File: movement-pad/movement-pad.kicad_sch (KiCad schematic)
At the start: 33 parts, among them U1 74LS147, U2 74LS42

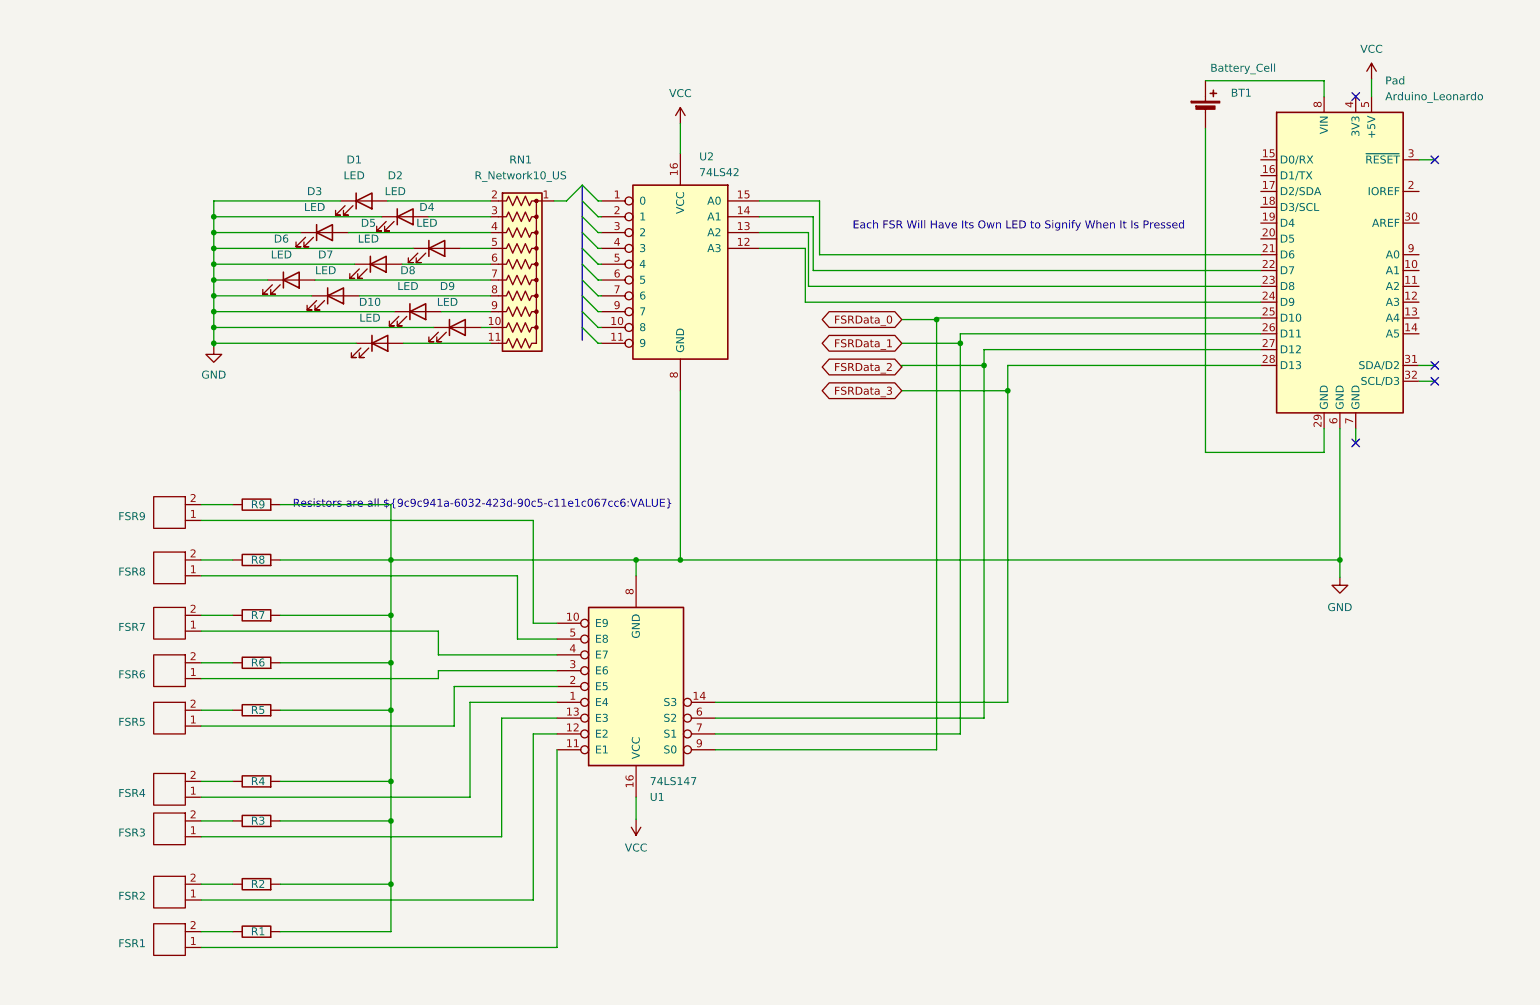
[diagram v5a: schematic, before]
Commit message: realized i screwed up with movement pad, redid it
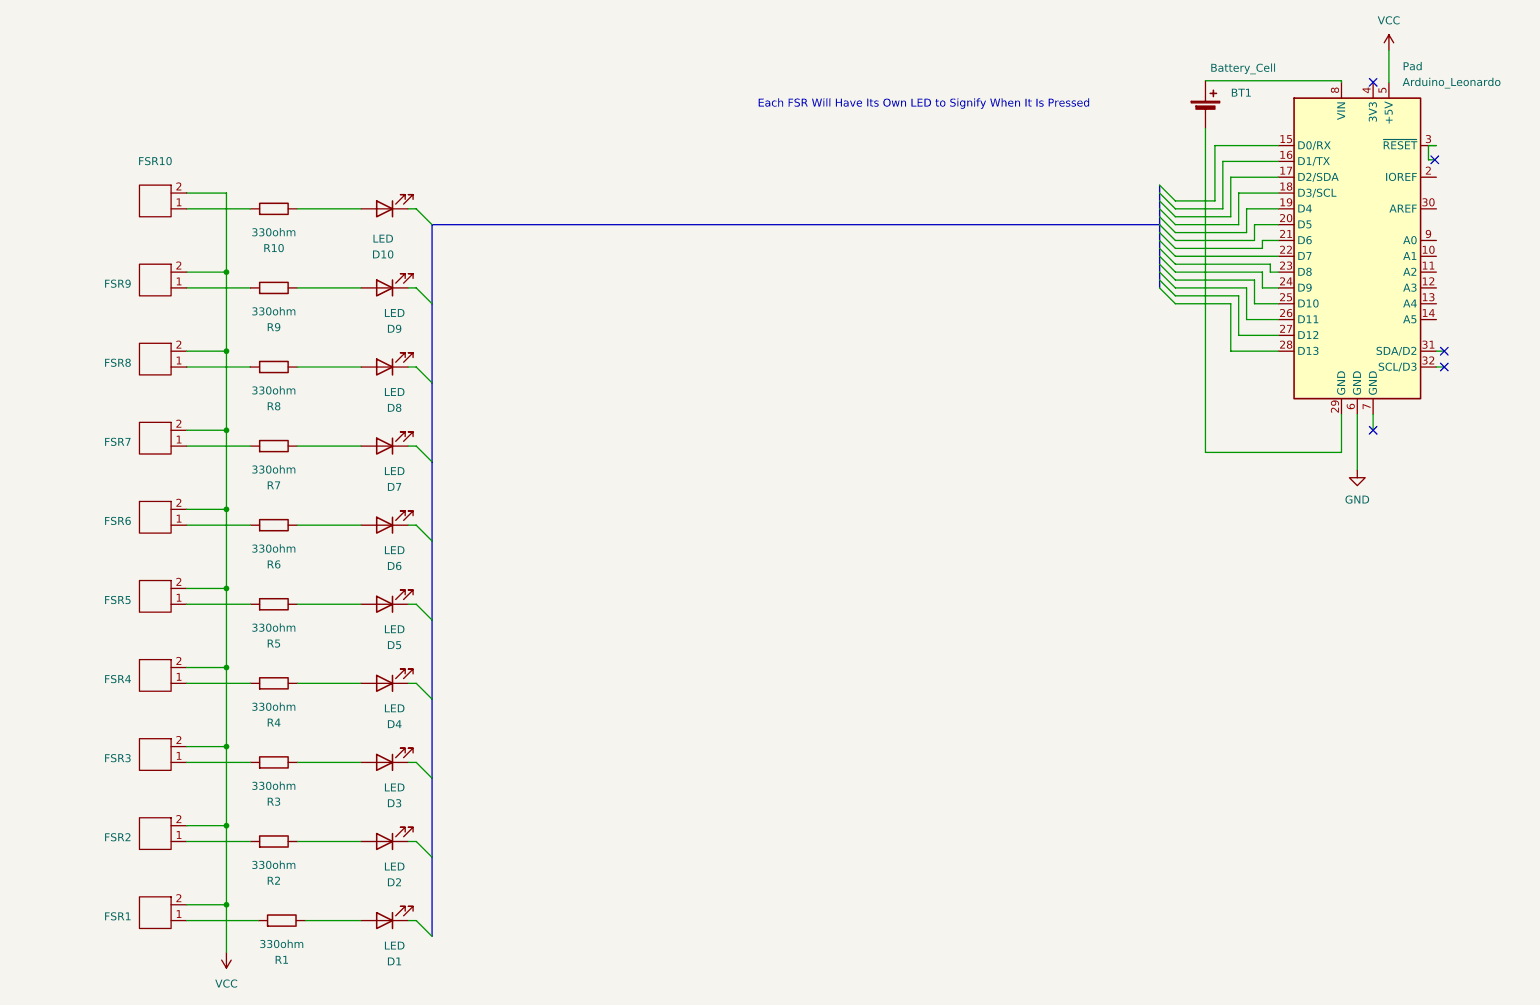
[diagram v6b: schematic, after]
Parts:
- removed R1, R2, R3, R4, R5, R6, R7, R8, R9: 390ohm, Resistor_THT:R_Axial_DIN0207_L6.3mm_D2.5mm_P10.16mm_Horizontal, symbol PCM_SL_Resistors:390ohm
- removed RN1: R_Network10_US, Resistor_THT:R_Array_SIP11, symbol Device:R_Network10_US
- removed U1: 74LS147, symbol 74xx:74LS147
- removed U2: 74LS42, symbol 74xx:74LS42
- added FSR10: ~, symbol GunProject_lib:FSR
- added R1, R10, R2, R3, R4, R5, R6, R7, R8, R9: 330ohm, Resistor_THT:R_Axial_DIN0207_L6.3mm_D2.5mm_P10.16mm_Horizontal, symbol PCM_SL_Resistors:330ohm
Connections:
- net GND: no longer D1.1 (K), D10.1 (K), D2.1 (K), D3.1 (K), D4.1 (K), D5.1 (K), D6.1 (K), D7.1 (K), D8.1 (K), D9.1 (K)
- net VCC: now also FSR1.2, FSR2.2, FSR3.2, FSR4.2, FSR5.2, FSR6.2, FSR7.2, FSR8.2, FSR9.2, FSR10.2
- net at D9.2 (A): now also R9.2
- net at D5.2 (A): now also R5.2
- net at D7.2 (A): now also R7.2
- net at D2.2 (A): now also R2.2
- net at FSR3.1: now also R3.1
- net at FSR4.1: now also R4.1
- net at FSR9.1: now also R9.1
- net at FSR1.1: now also R1.1
- net at FSR2.1: now also R2.1
- net at FSR5.1: now also R5.1
- net at FSR6.1: now also R6.1
- net at FSR7.1: now also R7.1
- net at FSR8.1: now also R8.1
- net at D4.2 (A): now also R4.2
- net at D10.2 (A): now also R10.2
- net at D3.2 (A): now also R3.2
- net at D1.2 (A): now also R1.2
- net at D6.2 (A): now also R6.2
- net at D8.2 (A): now also R8.2
- net FSRData_0: no longer names the net of Pad.25 (D10)
- net FSRData_1: no longer names the net of Pad.26 (D11)
- net FSRData_2: no longer names the net of Pad.27 (D12)
- net FSRData_3: no longer names the net of Pad.28 (D13)
- new net: FSR10.1, R10.1
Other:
- note removed: "Resistors are all ${9c9c941a-6032-423d-90c5-c11e1c067cc6:VALUE}"
- moved on the sheet: D1, D10, D2, D3, D4, D5, D6, D7, D8, D9, FSR1, FSR2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

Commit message: Reworked pad schematic again because the hookup guides are annoying
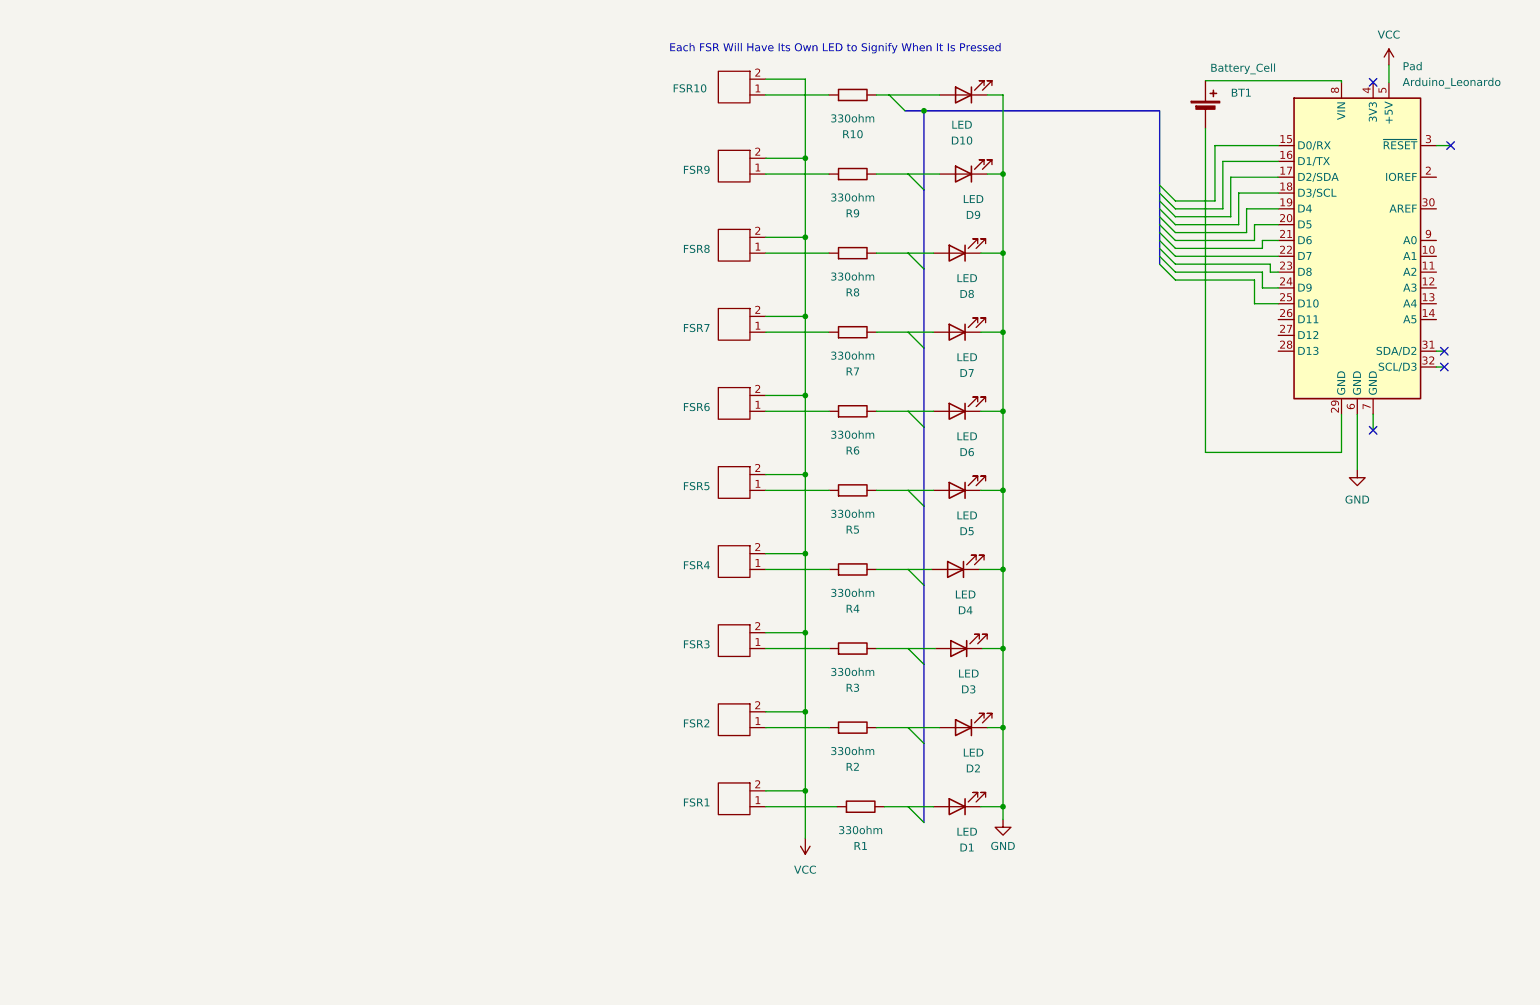
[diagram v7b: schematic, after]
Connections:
- net GND: now also D1.1 (K), D10.1 (K), D2.1 (K), D3.1 (K), D4.1 (K), D5.1 (K), D6.1 (K), D7.1 (K), D8.1 (K), D9.1 (K)
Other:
- moved on the sheet: D1, D10, D2, D3, D4, D5, D6, D7, D8, D9, FSR1, FSR10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
